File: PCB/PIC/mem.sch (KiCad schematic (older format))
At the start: 15 parts, among them U12 24AA1025, U13 24AA025E48, U20 SST26VF064BA, U24 23A1024

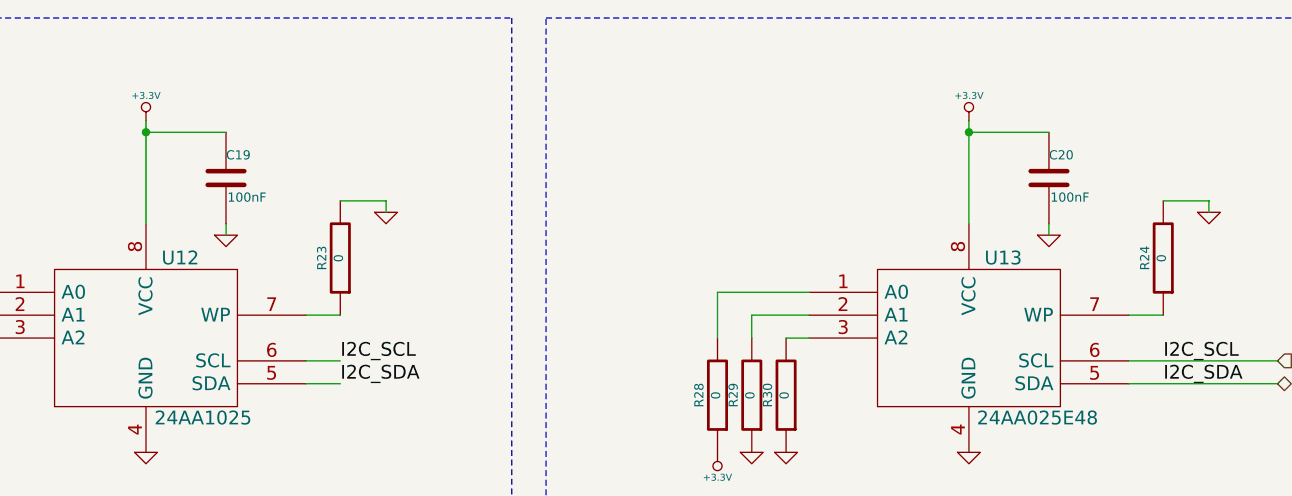
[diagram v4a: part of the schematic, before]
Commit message: elimino conector salida reles
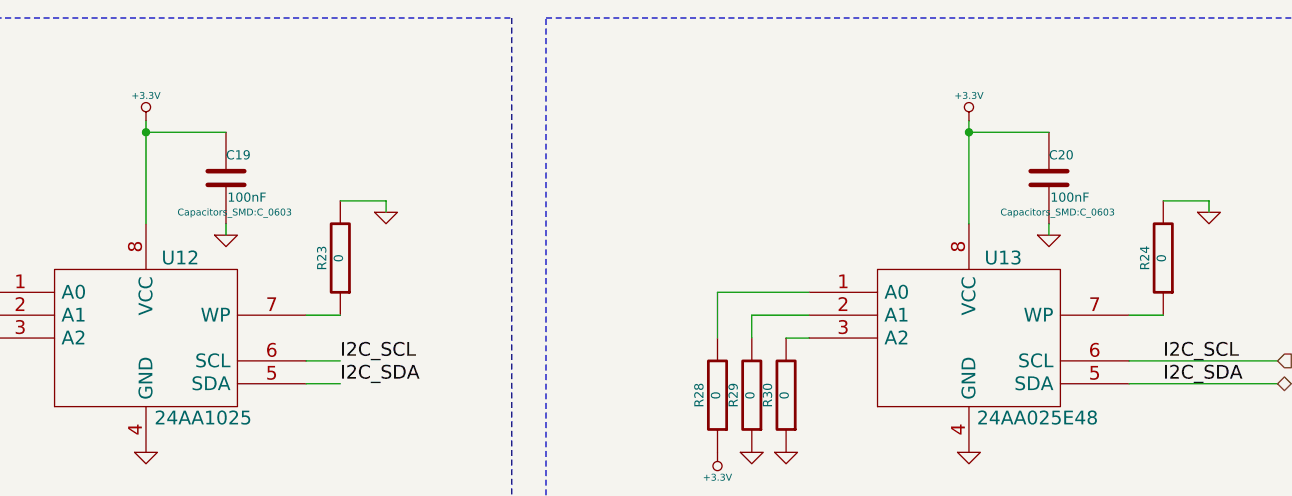
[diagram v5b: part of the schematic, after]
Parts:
- C19, C20, C45: footprint ~ -> Capacitors_SMD:C_0603
- R23, R24, R25, R26, R27, R28, R29, R30: footprint ~ -> Resistors_SMD:R_0603
- U20: footprint ~ -> (none)
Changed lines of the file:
@@
 F 0 "U12" H 5450 2900 60  0000 C CNN
 F 1 "24AA1025" H 5550 2200 60  0000 C CNN
-F 2 "" H 5300 2550 60  0000 C CNN
+F 2 "" H 5300 2550 60  0001 C CNN
 F 3 "" H 5300 2550 60  0000 C CNN
 	1    5300 2550
@@
 I2C_SCL
 $Comp
-L GND-RESCUE-ciaa-pic #PWR0174
+L GND-RESCUE-ciaa-pic #PWR0173
 U 1 1 52E536B1
 P 5300 3050
-F 0 "#PWR0174" H 5300 3050 30  0001 C CNN
+F 0 "#PWR0173" H 5300 3050 30  0001 C CNN
 F 1 "GND" H 5300 2980 30  0001 C CNN
 F 2 "" H 5300 3050 60  0000 C CNN
@@
 $EndComp
 $Comp
-L +3.3V-RESCUE-ciaa-pic #PWR0175
+L +3.3V-RESCUE-ciaa-pic #PWR0174
 U 1 1 52E536B7
 P 5300 1600
-F 0 "#PWR0175" H 5300 1560 30  0001 C CNN
+F 0 "#PWR0174" H 5300 1560 30  0001 C CNN
 F 1 "+3.3V" H 5300 1710 30  0000 C CNN
 F 2 "" H 5300 1600 60  0000 C CNN
@@
 F 0 "C19" H 5650 1950 40  0000 L CNN
 F 1 "100nF" H 5656 1765 40  0000 L CNN
-F 2 "~" H 5688 1700 30  0000 C CNN
+F 2 "Capacitors_SMD:C_0603" H 5688 1700 30  0000 C CNN
 F 3 "~" H 5650 1850 60  0000 C CNN
 	1    5650 1850
@@
 $EndComp
 $Comp
-L GND-RESCUE-ciaa-pic #PWR0176
+L GND-RESCUE-ciaa-pic #PWR0175
 U 1 1 52E536C5
 P 4350 3050
-F 0 "#PWR0176" H 4350 3050 30  0001 C CNN
+F 0 "#PWR0175" H 4350 3050 30  0001 C CNN
 F 1 "GND" H 4350 2980 30  0001 C CNN
 F 2 "" H 4350 3050 60  0000 C CNN
@@
 $EndComp
 $Comp
-L GND-RESCUE-ciaa-pic #PWR0177
+L GND-RESCUE-ciaa-pic #PWR0176
 U 1 1 52E536CB
 P 4200 3050
-F 0 "#PWR0177" H 4200 3050 30  0001 C CNN
+F 0 "#PWR0176" H 4200 3050 30  0001 C CNN
 F 1 "GND" H 4200 2980 30  0001 C CNN
 F 2 "" H 4200 3050 60  0000 C CNN
@@
 $EndComp
 $Comp
-L GND-RESCUE-ciaa-pic #PWR0178
+L GND-RESCUE-ciaa-pic #PWR0177
 U 1 1 52E536D1
 P 5650 2100
-F 0 "#PWR0178" H 5650 2100 30  0001 C CNN
+F 0 "#PWR0177" H 5650 2100 30  0001 C CNN
 F 1 "GND" H 5650 2030 30  0001 C CNN
 F 2 "" H 5650 2100 60  0000 C CNN
@@
 $EndComp
 $Comp
-L GND-RESCUE-ciaa-pic #PWR0179
+L GND-RESCUE-ciaa-pic #PWR0178
 U 1 1 52E536DF
 P 6350 2000
-F 0 "#PWR0179" H 6350 2000 30  0001 C CNN
+F 0 "#PWR0178" H 6350 2000 30  0001 C CNN
 F 1 "GND" H 6350 1930 30  0001 C CNN
 F 2 "" H 6350 2000 60  0000 C CNN
@@
 $EndComp
 $Comp
-L +3.3V-RESCUE-ciaa-pic #PWR0180
+L +3.3V-RESCUE-ciaa-pic #PWR0179
 U 1 1 52E536E8
 P 4500 3050
-F 0 "#PWR0180" H 4500 3010 30  0001 C CNN
+F 0 "#PWR0179" H 4500 3010 30  0001 C CNN
 F 1 "+3.3V" H 4500 3160 30  0000 C CNN
 F 2 "" H 4500 3050 60  0000 C CNN
@@
 F 0 "U13" H 9050 2900 60  0000 C CNN
 F 1 "24AA025E48" H 9200 2200 60  0000 C CNN
-F 2 "" H 8900 2550 60  0000 C CNN
+F 2 "" H 8900 2550 60  0001 C CNN
 F 3 "" H 8900 2550 60  0000 C CNN
 	1    8900 2550
@@
 I2C_SCL
 $Comp
-L GND-RESCUE-ciaa-pic #PWR0181
+L GND-RESCUE-ciaa-pic #PWR0180
 U 1 1 52E536F8
 P 8900 3050
-F 0 "#PWR0181" H 8900 3050 30  0001 C CNN
+F 0 "#PWR0180" H 8900 3050 30  0001 C CNN
 F 1 "GND" H 8900 2980 30  0001 C CNN
 F 2 "" H 8900 3050 60  0000 C CNN
@@
 $EndComp
 $Comp
-L +3.3V-RESCUE-ciaa-pic #PWR0182
+L +3.3V-RESCUE-ciaa-pic #PWR0181
 U 1 1 52E536FE
 P 8900 1600
-F 0 "#PWR0182" H 8900 1560 30  0001 C CNN
+F 0 "#PWR0181" H 8900 1560 30  0001 C CNN
 F 1 "+3.3V" H 8900 1710 30  0000 C CNN
 F 2 "" H 8900 1600 60  0000 C CNN
@@
 F 0 "C20" H 9250 1950 40  0000 L CNN
 F 1 "100nF" H 9256 1765 40  0000 L CNN
-F 2 "~" H 9288 1700 30  0000 C CNN
+F 2 "Capacitors_SMD:C_0603" H 9288 1700 30  0000 C CNN
 F 3 "~" H 9250 1850 60  0000 C CNN
 	1    9250 1850
@@
 $EndComp
 $Comp
-L GND-RESCUE-ciaa-pic #PWR0183
+L GND-RESCUE-ciaa-pic #PWR0182
 U 1 1 52E5370C
 P 7950 3050
-F 0 "#PWR0183" H 7950 3050 30  0001 C CNN
+F 0 "#PWR0182" H 7950 3050 30  0001 C CNN
 F 1 "GND" H 7950 2980 30  0001 C CNN
 F 2 "" H 7950 3050 60  0000 C CNN
@@
 $EndComp
 $Comp
-L GND-RESCUE-ciaa-pic #PWR0184
+L GND-RESCUE-ciaa-pic #PWR0183
 U 1 1 52E53712
 P 9250 2100
-F 0 "#PWR0184" H 9250 2100 30  0001 C CNN
+F 0 "#PWR0183" H 9250 2100 30  0001 C CNN
 F 1 "GND" H 9250 2030 30  0001 C CNN
 F 2 "" H 9250 2100 60  0000 C CNN
@@
 $EndComp
 $Comp
-L GND-RESCUE-ciaa-pic #PWR0185
+L GND-RESCUE-ciaa-pic #PWR0184
 U 1 1 52E5371B
 P 9950 2000
-F 0 "#PWR0185" H 9950 2000 30  0001 C CNN
+F 0 "#PWR0184" H 9950 2000 30  0001 C CNN
 F 1 "GND" H 9950 1930 30  0001 C CNN
 F 2 "" H 9950 2000 60  0000 C CNN
@@
 $EndComp
 $Comp
-L +3.3V-RESCUE-ciaa-pic #PWR0186
+L +3.3V-RESCUE-ciaa-pic #PWR0185
 U 1 1 52E53724
 P 7800 3050
-F 0 "#PWR0186" H 7800 3010 30  0001 C CNN
+F 0 "#PWR0185" H 7800 3010 30  0001 C CNN
 F 1 "+3.3V" H 7800 3160 30  0000 C CNN
 F 2 "" H 7800 3050 60  0000 C CNN
@@
 $EndComp
 $Comp
-L GND-RESCUE-ciaa-pic #PWR0187
+L GND-RESCUE-ciaa-pic #PWR0186
 U 1 1 52E5372A
 P 8100 3050
-F 0 "#PWR0187" H 8100 3050 30  0001 C CNN
+F 0 "#PWR0186" H 8100 3050 30  0001 C CNN
 F 1 "GND" H 8100 2980 30  0001 C CNN
 F 2 "" H 8100 3050 60  0000 C CNN
@@
 F 0 "R25" V 4280 2800 40  0000 C CNN
 F 1 "0" V 4207 2801 40  0000 C CNN
-F 2 "~" V 4130 2800 30  0000 C CNN
+F 2 "Resistors_SMD:R_0603" V 4130 2800 30  0001 C CNN
 F 3 "~" H 4200 2800 30  0000 C CNN
 	1    4200 2800
@@
 F 0 "R26" V 4430 2800 40  0000 C CNN
 F 1 "0" V 4357 2801 40  0000 C CNN
-F 2 "~" V 4280 2800 30  0000 C CNN
+F 2 "Resistors_SMD:R_0603" V 4280 2800 30  0001 C CNN
 F 3 "~" H 4350 2800 30  0000 C CNN
 	1    4350 2800
@@
 F 0 "R27" V 4580 2800 40  0000 C CNN
 F 1 "0" V 4507 2801 40  0000 C CNN
-F 2 "~" V 4430 2800 30  0000 C CNN
+F 2 "Resistors_SMD:R_0603" V 4430 2800 30  0001 C CNN
 F 3 "~" H 4500 2800 30  0000 C CNN
 	1    4500 2800
@@
 F 0 "R23" V 6230 2200 40  0000 C CNN
 F 1 "0" V 6157 2201 40  0000 C CNN
-F 2 "~" V 6080 2200 30  0000 C CNN
+F 2 "Resistors_SMD:R_0603" V 6080 2200 30  0001 C CNN
 F 3 "~" H 6150 2200 30  0000 C CNN
 	1    6150 2200
@@
 F 0 "R28" V 7880 2800 40  0000 C CNN
 F 1 "0" V 7807 2801 40  0000 C CNN
-F 2 "~" V 7730 2800 30  0000 C CNN
+F 2 "Resistors_SMD:R_0603" V 7730 2800 30  0001 C CNN
 F 3 "~" H 7800 2800 30  0000 C CNN
 	1    7800 2800
@@
 F 0 "R29" V 8030 2800 40  0000 C CNN
 F 1 "0" V 7957 2801 40  0000 C CNN
-F 2 "~" V 7880 2800 30  0000 C CNN
+F 2 "Resistors_SMD:R_0603" V 7880 2800 30  0001 C CNN
 F 3 "~" H 7950 2800 30  0000 C CNN
 	1    7950 2800
@@
 F 0 "R30" V 8180 2800 40  0000 C CNN
 F 1 "0" V 8107 2801 40  0000 C CNN
-F 2 "~" V 8030 2800 30  0000 C CNN
+F 2 "Resistors_SMD:R_0603" V 8030 2800 30  0001 C CNN
 F 3 "~" H 8100 2800 30  0000 C CNN
 	1    8100 2800
@@
 F 0 "R24" V 9830 2200 40  0000 C CNN
 F 1 "0" V 9757 2201 40  0000 C CNN
-F 2 "~" V 9680 2200 30  0000 C CNN
+F 2 "Resistors_SMD:R_0603" V 9680 2200 30  0001 C CNN
 F 3 "~" H 9750 2200 30  0000 C CNN
 	1    9750 2200
@@
 F 0 "C45" H 6700 5350 40  0000 L CNN
 F 1 "100nF" H 6706 5165 40  0000 L CNN
-F 2 "~" H 6738 5100 30  0000 C CNN
+F 2 "Capacitors_SMD:C_0603" H 6738 5100 30  0001 C CNN
 F 3 "~" H 6700 5250 60  0000 C CNN
 	1    6700 5250
@@
 $EndComp
 $Comp
-L +3.3V-RESCUE-ciaa-pic #PWR0188
+L +3.3V-RESCUE-ciaa-pic #PWR0187
 U 1 1 52E5407E
 P 6700 4950
-F 0 "#PWR0188" H 6700 4910 30  0001 C CNN
+F 0 "#PWR0187" H 6700 4910 30  0001 C CNN
 F 1 "+3.3V" H 6700 5060 30  0000 C CNN
 F 2 "" H 6700 4950 60  0000 C CNN
@@
 $EndComp
 $Comp
-L GND-RESCUE-ciaa-pic #PWR0189
+L GND-RESCUE-ciaa-pic #PWR0188
 U 1 1 52E540A7
 P 6700 5550
-F 0 "#PWR0189" H 6700 5550 30  0001 C CNN
+F 0 "#PWR0188" H 6700 5550 30  0001 C CNN
 F 1 "GND" H 6700 5480 30  0001 C CNN
 F 2 "" H 6700 5550 60  0000 C CNN
@@
 F 0 "U20" H 5400 5650 60  0000 C CNN
 F 1 "SST26VF064BA" H 5850 4800 60  0000 C CNN
-F 2 "~" H 5800 5050 60  0000 C CNN
+F 2 "" H 5800 5050 60  0001 C CNN
 F 3 "~" H 5800 5050 60  0000 C CNN
 	1    5800 5250
@@
 $EndComp
 $Comp
-L GND-RESCUE-ciaa-pic #PWR0190
+L GND-RESCUE-ciaa-pic #PWR0189
 U 1 1 577B0CE8
 P 2000 3200
-F 0 "#PWR0190" H 2000 3200 30  0001 C CNN
+F 0 "#PWR0189" H 2000 3200 30  0001 C CNN
 F 1 "GND" H 2000 3130 30  0001 C CNN
 F 2 "" H 2000 3200 60  0000 C CNN
@@
 $EndComp
 $Comp
-L +3.3V-RESCUE-ciaa-pic #PWR0191
+L +3.3V-RESCUE-ciaa-pic #PWR0190
 U 1 1 577B0CEE
 P 2000 1500
-F 0 "#PWR0191" H 2000 1460 30  0001 C CNN
+F 0 "#PWR0190" H 2000 1460 30  0001 C CNN
 F 1 "+3.3V" H 2000 1610 30  0000 C CNN
 F 2 "" H 2000 1500 60  0000 C CNN

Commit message: rev02 CIAA-PIC
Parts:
- removed R25, R26, R27, R28, R29, R30: 0, Resistors_SMD:R_0603, symbol R-RESCUE-ciaa-pic
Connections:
- net +3.3V: now also U12.3 (A2), U13.1 (A0)
- net GND: now also U12.1 (A0), U12.2 (A1), U13.2 (A1), U13.3 (A2)
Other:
- note removed: "Aclararía para que esta cada una de las R de 0 Ohm."
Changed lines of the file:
@@
-$EndComp
-$Comp
-L R-RESCUE-ciaa-pic R25
-U 1 1 52E53730
-P 4200 2800
-F 0 "R25" V 4280 2800 40  0000 C CNN
-F 1 "0" V 4207 2801 40  0000 C CNN
-F 2 "Resistors_SMD:R_0603" V 4130 2800 30  0001 C CNN
-F 3 "~" H 4200 2800 30  0000 C CNN
-	1    4200 2800
-	-1   0    0    1
-$EndComp
-$Comp
-L R-RESCUE-ciaa-pic R26
-U 1 1 52E53736
-P 4350 2800
-F 0 "R26" V 4430 2800 40  0000 C CNN
-F 1 "0" V 4357 2801 40  0000 C CNN
-F 2 "Resistors_SMD:R_0603" V 4280 2800 30  0001 C CNN
-F 3 "~" H 4350 2800 30  0000 C CNN
-	1    4350 2800
-	-1   0    0    1
-$EndComp
-$Comp
-L R-RESCUE-ciaa-pic R27
-U 1 1 52E5373C
-P 4500 2800
-F 0 "R27" V 4580 2800 40  0000 C CNN
-F 1 "0" V 4507 2801 40  0000 C CNN
-F 2 "Resistors_SMD:R_0603" V 4430 2800 30  0001 C CNN
-F 3 "~" H 4500 2800 30  0000 C CNN
-	1    4500 2800
-	-1   0    0    1
 $EndComp
 $Comp
@@
 F 3 "~" H 6150 2200 30  0000 C CNN
 	1    6150 2200
-	-1   0    0    1
-$EndComp
-$Comp
-L R-RESCUE-ciaa-pic R28
-U 1 1 52E5374D
-P 7800 2800
-F 0 "R28" V 7880 2800 40  0000 C CNN
-F 1 "0" V 7807 2801 40  0000 C CNN
-F 2 "Resistors_SMD:R_0603" V 7730 2800 30  0001 C CNN
-F 3 "~" H 7800 2800 30  0000 C CNN
-	1    7800 2800
-	-1   0    0    1
-$EndComp
-$Comp
-L R-RESCUE-ciaa-pic R29
-U 1 1 52E53753
-P 7950 2800
-F 0 "R29" V 8030 2800 40  0000 C CNN
-F 1 "0" V 7957 2801 40  0000 C CNN
-F 2 "Resistors_SMD:R_0603" V 7880 2800 30  0001 C CNN
-F 3 "~" H 7950 2800 30  0000 C CNN
-	1    7950 2800
-	-1   0    0    1
-$EndComp
-$Comp
-L R-RESCUE-ciaa-pic R30
-U 1 1 52E53759
-P 8100 2800
-F 0 "R30" V 8180 2800 40  0000 C CNN
-F 1 "0" V 8107 2801 40  0000 C CNN
-F 2 "Resistors_SMD:R_0603" V 8030 2800 30  0001 C CNN
-F 3 "~" H 8100 2800 30  0000 C CNN
-	1    8100 2800
 	-1   0    0    1
 $EndComp
@@
 	4600 2350 4200 2350
 Wire Wire Line
-	4200 2350 4200 2550
+	4200 2350 4200 3050
 Wire Wire Line
 	4600 2450 4350 2450
 Wire Wire Line
-	4350 2450 4350 2550
+	4350 2450 4350 3050
 Wire Wire Line
 	4500 2550 4600 2550
@@
 	8200 2350 7800 2350
 Wire Wire Line
-	7800 2350 7800 2550
+	7800 2350 7800 3050
 Wire Wire Line
 	8200 2450 7950 2450
 Wire Wire Line
-	7950 2450 7950 2550
+	7950 2450 7950 3050
 Wire Wire Line
 	8100 2550 8200 2550
@@
 Wire Notes Line
 	7050 3700 7050 1150
-Text Notes 950  8300 0    200  ~ 0
-Aclararía para que esta cada una de las R de 0 Ohm.
 $Comp
 L 23A1024 U24
@@
 Wire Notes Line
 	650  1150 1050 1150
+Wire Wire Line
+	4500 2550 4500 3050
+Wire Wire Line
+	8100 2550 8100 3050
 $EndSCHEMATC

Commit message: rev.02 CIAA-PIC
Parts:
- C19, C20, C45: #manf (none) -> C0603C104K5RACTU
- R23, R24: #Digikey (none) -> 311-0.0GRCT-ND; #manf (none) -> RC0603JR-070RL
- U12: footprint (none) -> SMD_Packages:SOIC-8-N; #manf (none) -> 24AA1025T-I/SN
- U13: footprint (none) -> SMD_Packages:SOIC-8-N; #manf (none) -> 24AA025E48T-I/SN
- U20: #manf (none) -> SST26VF064BAT-104I/SM
- U24: #manf (none) -> 23A1024-I/SN
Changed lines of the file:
@@
 F 0 "U12" H 5450 2900 60  0000 C CNN
 F 1 "24AA1025" H 5550 2200 60  0000 C CNN
-F 2 "" H 5300 2550 60  0001 C CNN
+F 2 "SMD_Packages:SOIC-8-N" H 5300 2550 60  0001 C CNN
 F 3 "" H 5300 2550 60  0000 C CNN
+F 4 "24AA1025T-I/SN" H 5300 2550 60  0001 C CNN "#manf"
 	1    5300 2550
 	1    0    0    -1
@@
 F 0 "C19" H 5650 1950 40  0000 L CNN
 F 1 "100nF" H 5656 1765 40  0000 L CNN
-F 2 "Capacitors_SMD:C_0603" H 5688 1700 30  0000 C CNN
+F 2 "Capacitors_SMD:C_0603" H 5688 1700 30  0001 C CNN
 F 3 "~" H 5650 1850 60  0000 C CNN
+F 4 "C0603C104K5RACTU " H 5650 1850 60  0001 C CNN "#manf"
 	1    5650 1850
 	1    0    0    -1
@@
 F 0 "U13" H 9050 2900 60  0000 C CNN
 F 1 "24AA025E48" H 9200 2200 60  0000 C CNN
-F 2 "" H 8900 2550 60  0001 C CNN
+F 2 "SMD_Packages:SOIC-8-N" H 8900 2550 60  0001 C CNN
 F 3 "" H 8900 2550 60  0000 C CNN
+F 4 "24AA025E48T-I/SN" H 8900 2550 60  0001 C CNN "#manf"
 	1    8900 2550
 	1    0    0    -1
@@
 F 0 "C20" H 9250 1950 40  0000 L CNN
 F 1 "100nF" H 9256 1765 40  0000 L CNN
-F 2 "Capacitors_SMD:C_0603" H 9288 1700 30  0000 C CNN
+F 2 "Capacitors_SMD:C_0603" H 9288 1700 30  0001 C CNN
 F 3 "~" H 9250 1850 60  0000 C CNN
+F 4 "C0603C104K5RACTU " H 9250 1850 60  0001 C CNN "#manf"
 	1    9250 1850
 	1    0    0    -1
@@
 F 2 "Resistors_SMD:R_0603" V 6080 2200 30  0001 C CNN
 F 3 "~" H 6150 2200 30  0000 C CNN
+F 4 "RC0603JR-070RL" V 6150 2200 60  0001 C CNN "#manf"
+F 5 " 311-0.0GRCT-ND" V 6150 2200 60  0001 C CNN "#Digikey"
 	1    6150 2200
 	-1   0    0    1
@@
 F 2 "Resistors_SMD:R_0603" V 9680 2200 30  0001 C CNN
 F 3 "~" H 9750 2200 30  0000 C CNN
+F 4 "311-0.0GRCT-ND" V 9750 2200 60  0001 C CNN "#Digikey"
+F 5 "RC0603JR-070RL" V 9750 2200 60  0001 C CNN "#manf"
 	1    9750 2200
 	-1   0    0    1
@@
 F 2 "Capacitors_SMD:C_0603" H 6738 5100 30  0001 C CNN
 F 3 "~" H 6700 5250 60  0000 C CNN
+F 4 "C0603C104K5RACTU " H 6700 5250 60  0001 C CNN "#manf"
 	1    6700 5250
 	1    0    0    -1
@@
 F 2 "" H 5800 5050 60  0001 C CNN
 F 3 "~" H 5800 5050 60  0000 C CNN
+F 4 "SST26VF064BAT-104I/SM" H 5800 5250 60  0001 C CNN "#manf"
 	1    5800 5250
 	1    0    0    -1
@@
 F 2 "footprints:-SOIC8" H 1450 1700 60  0001 C CNN
 F 3 "http://www.digikey.com/product-detail/es/23A1024-I%2FSN/23A1024-I%2FSN-ND/3543081" H 1950 1150 60  0001 C CNN
+F 4 "23A1024-I/SN " H 2000 2300 60  0001 C CNN "#manf"
 	1    2000 2300
 	1    0    0    -1
